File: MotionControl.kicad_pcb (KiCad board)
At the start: 2 copper layers, 180 x 80 mm, 180 parts, among them J1 Screw_Terminal_01x02, J10 Screw_Terminal_01x02, J11 Screw_Terminal_01x02, J12 Conn_01x07_MountingPin, J13 Conn_01x07_MountingPin, J14 Conn_01x07_MountingPin, J2 Conn_ARM_JTAG_SWD_10, J3 Screw_Terminal_01x04, J4 Conn_01x07_MountingPin, J5 Screw_Terminal_01x04, J6 Screw_Terminal_01x04, J7 Screw_Terminal_01x04, J8 Screw_Terminal_01x02, J9 Screw_Terminal_01x02, P1 USB_C_Plug_USB2.0, Q1 2N7002, Q10 Q_NMOS_DGS, Q11 Q_NMOS_DGS, Q12 Q_NMOS_DGS, Q13 Q_NMOS_DGS, Q14 Q_NMOS_DGS, Q15 Q_NMOS_DGS, Q16 Q_NMOS_DGS, Q17 Q_NMOS_DGS, Q18 Q_NMOS_DGS, Q19 Q_NMOS_DGS, Q2 Q_NMOS_DGS, Q20 Q_NMOS_DGS, Q21 Q_NMOS_DGS, Q22 Q_NMOS_DGS, Q23 Q_NMOS_DGS, Q24 Q_NMOS_DGS, Q25 Q_NMOS_DGS, Q26 Q_NMOS_DGS, Q27 Q_NMOS_DGS, Q28 Q_NMOS_DGS, Q29 Q_NMOS_DGS, Q3 Q_NMOS_DGS, Q30 Q_NMOS_DGS, Q31 Q_NMOS_DGS, Q32 Q_NMOS_DGS, Q33 Q_NMOS_DGS, Q4 Q_NMOS_DGS, Q5 Q_NMOS_DGS, Q6 Q_NMOS_DGS, Q7 Q_NMOS_DGS, Q8 Q_NMOS_DGS, Q9 Q_NMOS_DGS, SW1 SW_Push, U1 ATSAMD21J18A-A, U2 AP2112K-3.3, U3 TMC5160A-TA, U4 TMC5160A-TA, U5 TMC5160A-TA, U6 TMC5160A-TA, U7 TC4427, Y1 32.768kHz

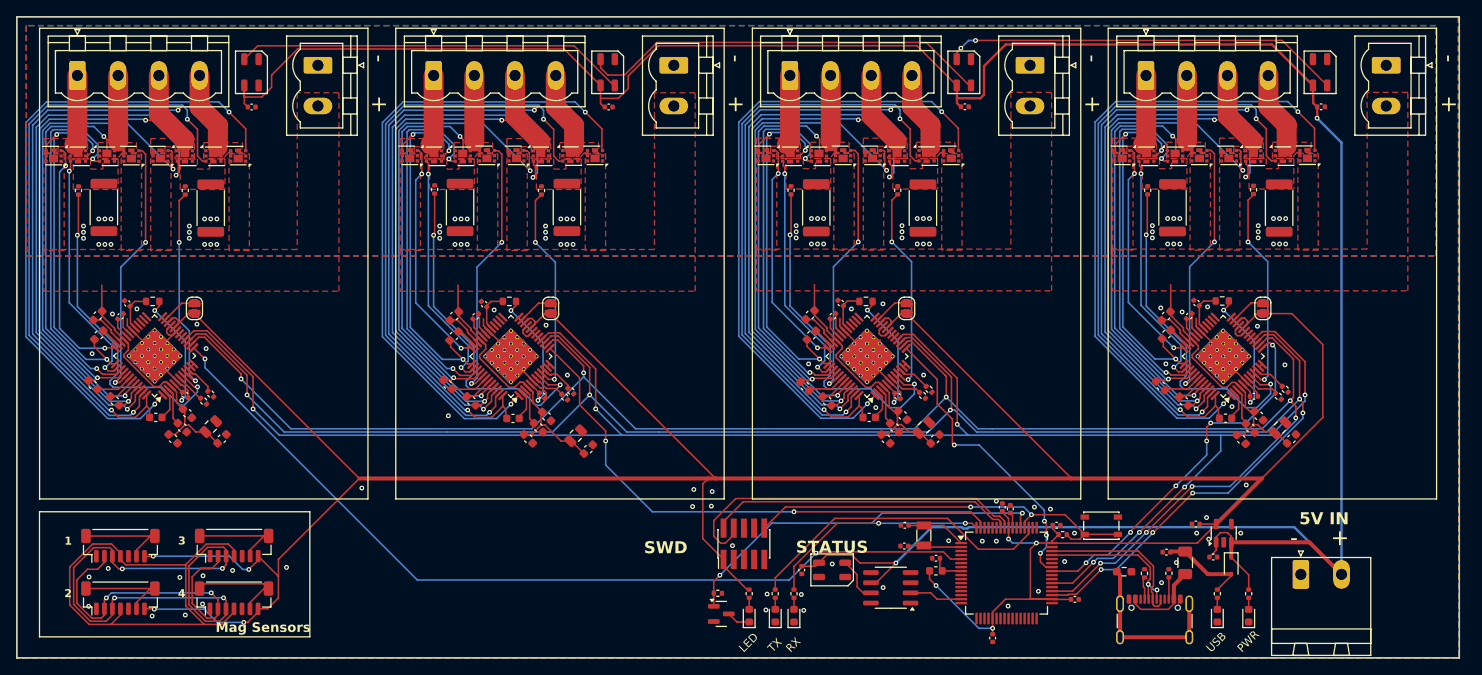
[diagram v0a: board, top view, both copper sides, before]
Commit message: begin work on optical inputs, finish mag sensors
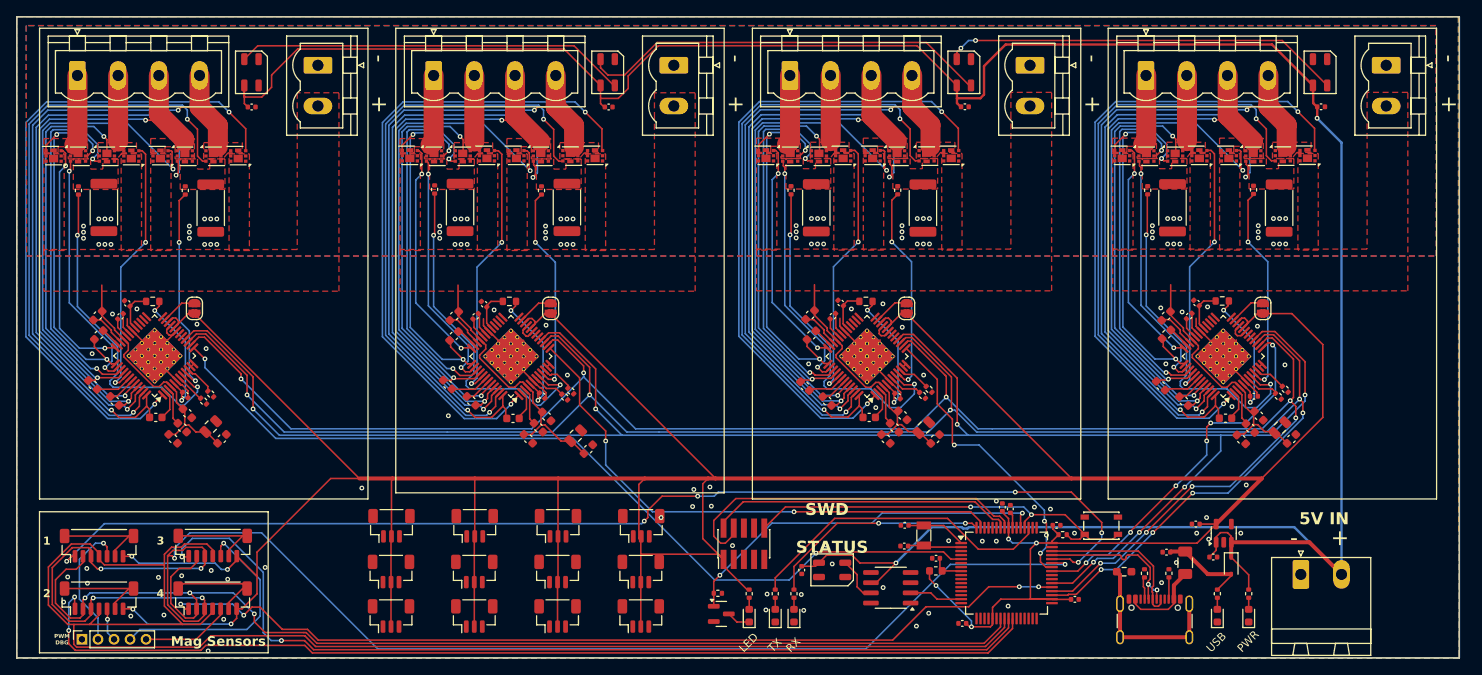
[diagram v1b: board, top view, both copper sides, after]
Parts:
- added J15: Conn_01x05_Pin, Connector_PinSocket_2.00mm:PinSocket_1x05_P2.00mm_Vertical, F.Cu at (41.1, 98.0)
- added J16: Conn_01x03_MountingPin, Connector_JST:JST_SH_BM03B-SRSS-TB_1x03-1MP_P1.00mm_Vertical, F.Cu at (79.8, 83.8)
- added J17: Conn_01x03_MountingPin, Connector_JST:JST_SH_BM03B-SRSS-TB_1x03-1MP_P1.00mm_Vertical, F.Cu at (79.7, 89.5)
- added J18: Conn_01x03_MountingPin, Connector_JST:JST_SH_BM03B-SRSS-TB_1x03-1MP_P1.00mm_Vertical, F.Cu at (79.7, 95.1)
- added J19: Conn_01x03_MountingPin, Connector_JST:JST_SH_BM03B-SRSS-TB_1x03-1MP_P1.00mm_Vertical, F.Cu at (90.2, 83.8)
- added J20: Conn_01x03_MountingPin, Connector_JST:JST_SH_BM03B-SRSS-TB_1x03-1MP_P1.00mm_Vertical, F.Cu at (90.1, 89.5)
- added J21: Conn_01x03_MountingPin, Connector_JST:JST_SH_BM03B-SRSS-TB_1x03-1MP_P1.00mm_Vertical, F.Cu at (90.1, 95.1)
- added J22: Conn_01x03_MountingPin, Connector_JST:JST_SH_BM03B-SRSS-TB_1x03-1MP_P1.00mm_Vertical, F.Cu at (100.6, 83.8)
- added J23: Conn_01x03_MountingPin, Connector_JST:JST_SH_BM03B-SRSS-TB_1x03-1MP_P1.00mm_Vertical, F.Cu at (100.5, 89.5)
- added J24: Conn_01x03_MountingPin, Connector_JST:JST_SH_BM03B-SRSS-TB_1x03-1MP_P1.00mm_Vertical, F.Cu at (100.5, 95.1)
- added J25: Conn_01x03_MountingPin, Connector_JST:JST_SH_BM03B-SRSS-TB_1x03-1MP_P1.00mm_Vertical, F.Cu at (110.9, 83.8)
- added J26: Conn_01x03_MountingPin, Connector_JST:JST_SH_BM03B-SRSS-TB_1x03-1MP_P1.00mm_Vertical, F.Cu at (110.9, 89.5)
- added J27: Conn_01x03_MountingPin, Connector_JST:JST_SH_BM03B-SRSS-TB_1x03-1MP_P1.00mm_Vertical, F.Cu at (110.9, 95.1)
- R8, R9: value 130R -> 165R
- moved C10 4.20 mm to (151.0, 96.0), turned to 180 degrees
- moved J12 2.67 mm to (57.5, 92.9)
- moved J13 2.67 mm to (43.3, 86.3)
- moved J14 2.67 mm to (43.3, 92.9)
- moved J4 2.67 mm to (57.5, 86.3)
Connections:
- J12 pad 1: /Mag Sensors/CSn4 -> PA18_MAG_CSn4
- J12 pad 2: /Mag Sensors/MOSI -> PB10_MAG_MOSI
- J12 pad 3: /Mag Sensors/MISO -> PA22_MAG_MISO
- J12 pad 4: /Mag Sensors/CLK -> PB11_MAG_SCK
- J13 pad 1: /Mag Sensors/CSn1 -> PA23_MAG_CSn1
- J13 pad 2: /Mag Sensors/MOSI -> PB10_MAG_MOSI
- J13 pad 3: /Mag Sensors/MISO -> PA22_MAG_MISO
- J13 pad 4: /Mag Sensors/CLK -> PB11_MAG_SCK
- J14 pad 1: /Mag Sensors/CSn2 -> PB13_MAG_CSn2
- J14 pad 2: /Mag Sensors/MOSI -> PB10_MAG_MOSI
- J14 pad 3: /Mag Sensors/MISO -> PA22_MAG_MISO
- J14 pad 4: /Mag Sensors/CLK -> PB11_MAG_SCK
- J4 pad 1: /Mag Sensors/CSn3 -> PB12_MAG_CSn3
- J4 pad 2: /Mag Sensors/MOSI -> PB10_MAG_MOSI
- J4 pad 3: /Mag Sensors/MISO -> PA22_MAG_MISO
- J4 pad 4: /Mag Sensors/CLK -> PB11_MAG_SCK
- U1 pad 23: unconnected-(U1-PB10-Pad23) -> PB10_MAG_MOSI
- U1 pad 24: unconnected-(U1-PB11-Pad24) -> PB11_MAG_SCK
- U1 pad 25: unconnected-(U1-PB12-Pad25) -> PB12_MAG_CSn3
- U1 pad 26: unconnected-(U1-PB13-Pad26) -> PB13_MAG_CSn2
- U1 pad 37: unconnected-(U1-PA18-Pad37) -> PA18_MAG_CSn4
- U1 pad 43: unconnected-(U1-PA22-Pad43) -> PA22_MAG_MISO
- U1 pad 44: unconnected-(U1-PA23-Pad44) -> PA23_MAG_CSn1
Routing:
- net PA22_MAG_MISO: track 0.00 -> 196.2 mm, vias 0 -> 6
- net PB11_MAG_SCK: track 0.00 -> 186.3 mm
- net PB10_MAG_MOSI: track 0.00 -> 149.5 mm, vias 0 -> 3
- net PA23_MAG_CSn1: track 0.00 -> 145.8 mm, vias 0 -> 6
- net PB13_MAG_CSn2: track 0.00 -> 128.9 mm, vias 0 -> 2
- net PB12_MAG_CSn3: track 0.00 -> 118.1 mm, vias 0 -> 2
- net PA18_MAG_CSn4: track 0.00 -> 115.4 mm, vias 0 -> 4
- net +3V3: track 405.9 -> 497.2 mm
- net /Mag Sensors/MISO: track 69.2 -> 0.00 mm, vias 4 -> 0
- net /Mag Sensors/CLK: track 63.6 -> 0.00 mm
- net /Mag Sensors/MOSI: track 43.3 -> 0.00 mm, vias 2 -> 0
- net /Mag Sensors/PWM3: track 0.00 -> 30.2 mm, vias 0 -> 1
- net /Mag Sensors/PWM1: track 0.00 -> 16.6 mm, vias 0 -> 1
- net /Mag Sensors/PWM4: track 0.00 -> 11.3 mm
- net /Mag Sensors/PWM2: track 0.00 -> 4.17 mm, vias 0 -> 1
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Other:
- board text added: "PWM DBG"

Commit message: cs routing changes, endstop stuff
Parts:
- moved J16 10.4 mm to (69.4, 83.8)
- moved J19 10.4 mm to (79.7, 83.8)
- moved J22 10.4 mm to (90.1, 83.8)
- moved J17 10.4 mm to (69.3, 89.5)
- moved J18 10.4 mm to (69.3, 95.1)
- moved J20 10.4 mm to (79.7, 89.5)
- moved J21 10.4 mm to (79.7, 95.1)
- moved J23 10.4 mm to (90.1, 89.5)
- moved J24 10.4 mm to (90.1, 95.1)
- moved J25 10.4 mm to (100.5, 83.8)
- moved J26 10.4 mm to (100.5, 89.5)
- moved J27 10.4 mm to (100.5, 95.1)
- moved C7 0.47 mm to (156.0, 81.1)
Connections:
- J13 pad 1: PA23_MAG_CSn1 -> PB30_MAG_CSn1
- J16 pad 3: /Optical Sensors/OUT1 -> PB00_ES1
- J17 pad 3: /Optical Sensors/OUT2 -> PB01_ES2
- J18 pad 3: /Optical Sensors/OUT3 -> PB05_ES3
- J19 pad 3: /Optical Sensors/OUT4 -> PB06_ES4
- J20 pad 3: /Optical Sensors/OUT5 -> PB07_ES5
- J21 pad 3: /Optical Sensors/OUT6 -> PB08_ES6
- J22 pad 3: /Optical Sensors/OUT7 -> PB06_ES7
- J23 pad 3: /Optical Sensors/OUT8 -> PB15_ES8
- J24 pad 3: /Optical Sensors/OUT9 -> PB16_ES9
- J25 pad 3: /Optical Sensors/OUT10 -> PB17_ES10
- J26 pad 3: /Optical Sensors/OUT11 -> PB22_ES11
- J27 pad 3: /Optical Sensors/OUT12 -> PB23_ES12
- U1 pad 10: unconnected-(U1-PB07-Pad10) -> PB07_ES5
- U1 pad 11: unconnected-(U1-PB08-Pad11) -> PB08_ES6
- U1 pad 12: unconnected-(U1-PB09-Pad12) -> PB06_ES7
- U1 pad 27: unconnected-(U1-PB14-Pad27) -> PA18_MAG_CSn4
- U1 pad 28: unconnected-(U1-PB15-Pad28) -> PB15_ES8
- U1 pad 37: PA18_MAG_CSn4 -> unconnected-(U1-PA18-Pad37)
- U1 pad 39: unconnected-(U1-PB16-Pad39) -> PB16_ES9
- U1 pad 40: unconnected-(U1-PB17-Pad40) -> PB17_ES10
- U1 pad 44: PA23_MAG_CSn1 -> unconnected-(U1-PA23-Pad44)
- U1 pad 49: unconnected-(U1-PB22-Pad49) -> PB22_ES11
- U1 pad 50: unconnected-(U1-PB23-Pad50) -> PB23_ES12
- U1 pad 59: unconnected-(U1-PB30-Pad59) -> PB30_MAG_CSn1
- U1 pad 6: unconnected-(U1-PB05-Pad6) -> PB05_ES3
- U1 pad 61: unconnected-(U1-PB00-Pad61) -> PB00_ES1
- U1 pad 62: unconnected-(U1-PB01-Pad62) -> PB01_ES2
- U1 pad 9: unconnected-(U1-PB06-Pad9) -> PB06_ES4
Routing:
- net PA23_MAG_CSn1: track 145.8 -> 0.00 mm, vias 6 -> 0
- net PB30_MAG_CSn1: track 0.00 -> 124.6 mm, vias 0 -> 6
- net +3V3: track 497.2 -> 487.1 mm
- net PA18_MAG_CSn4: track 115.4 -> 111.9 mm
- net PA28_LED: track 47.1 -> 50.1 mm
- net /RESETn: track 51.8 -> 53.4 mm
- net PB10_MAG_MOSI: track 149.5 -> 148.9 mm
- net PB13_MAG_CSn2: track 128.9 -> 129.5 mm
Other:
- board text added: "Endstops"
- board text added: "Mag Encoders"
- board text removed: "Mag Sensors"

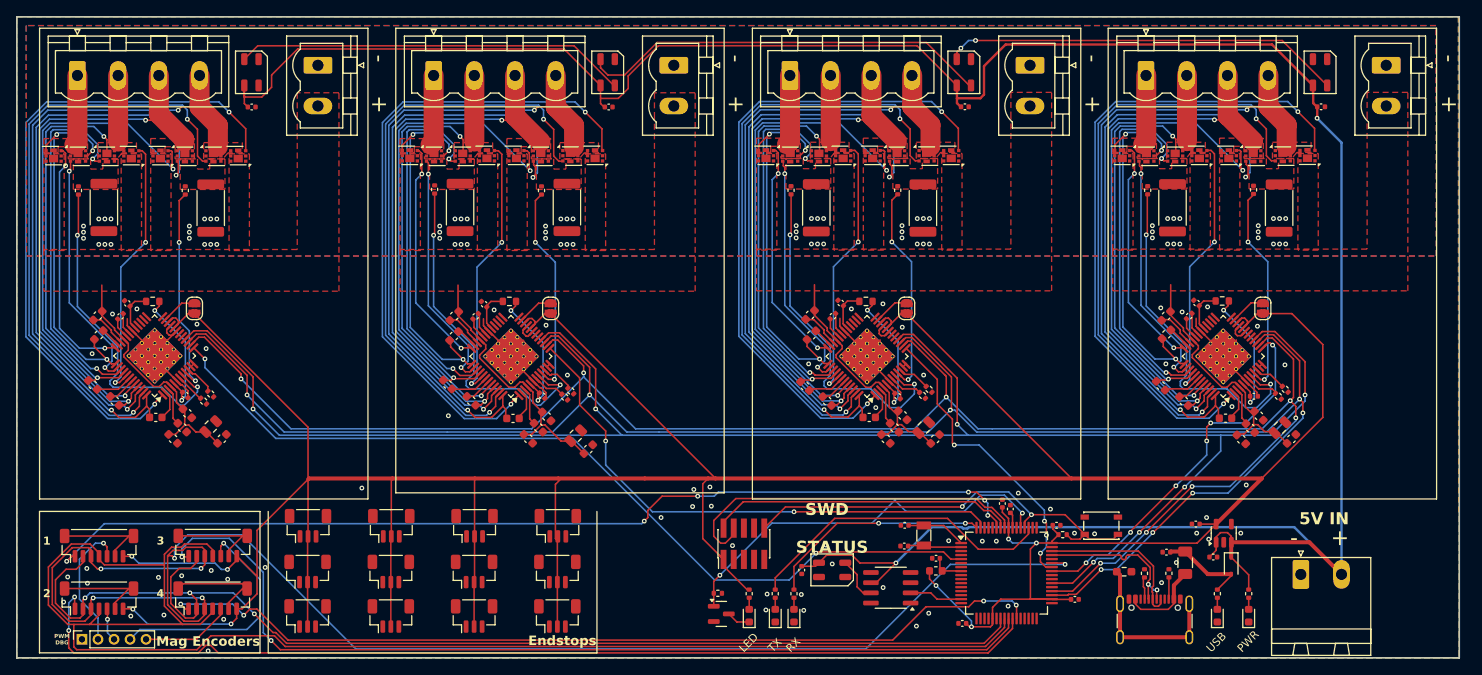
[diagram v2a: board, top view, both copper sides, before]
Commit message: route all endstops
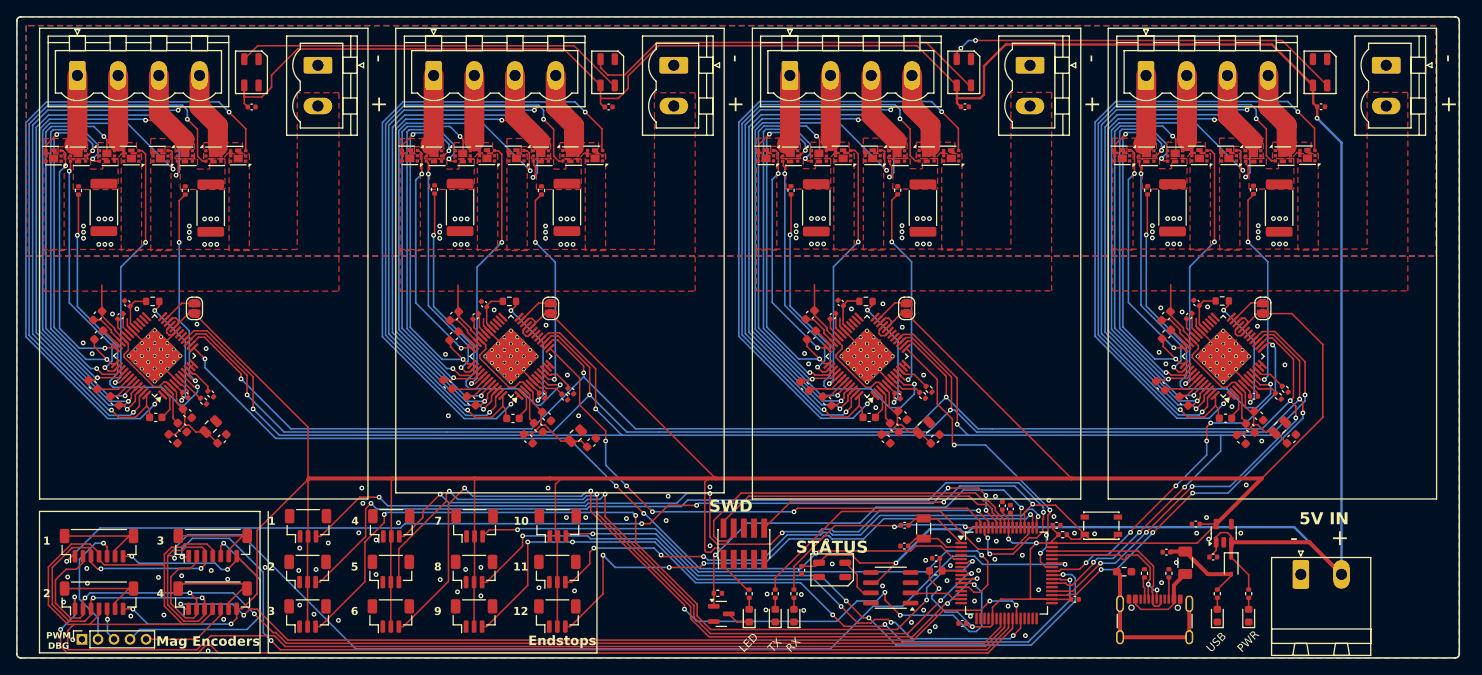
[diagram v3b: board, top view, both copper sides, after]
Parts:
- moved C48 0.92 mm to (104.7, 73.4)
- moved Y1 0.86 mm to (146.2, 84.2)
- moved C7 0.28 mm to (156.0, 81.3)
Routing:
- net PB01_ES2: track 0.00 -> 114.2 mm, vias 0 -> 4
- net PB08_ES6: track 0.00 -> 106.4 mm, vias 0 -> 6
- net PB05_ES3: track 0.00 -> 106.2 mm, vias 0 -> 4
- net PB00_ES1: track 0.00 -> 96.2 mm, vias 0 -> 4
- net PB07_ES5: track 0.00 -> 95.2 mm, vias 0 -> 4
- net PB16_ES9: track 0.00 -> 93.2 mm, vias 0 -> 5
- net PB06_ES4: track 0.00 -> 89.1 mm, vias 0 -> 4
- net PB15_ES8: track 0.00 -> 77.8 mm, vias 0 -> 4
- net PB17_ES10: track 0.00 -> 77.7 mm, vias 0 -> 4
- net PB06_ES7: track 0.00 -> 74.2 mm, vias 0 -> 2
- net PB23_ES12: track 0.00 -> 70.1 mm, vias 0 -> 4
- net PB22_ES11: track 0.00 -> 67.3 mm, vias 0 -> 4
- net /RESETn: track 53.4 -> 55.4 mm
- net +3V3: track 487.1 -> 489.0 mm
- net PA28_LED: track 50.1 -> 51.5 mm
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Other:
- outline, holes or cut-outs redrawn
- board text added: "10"
- board text added: "11"
- board text added: "12"
- board text added: "5"
- board text added: "6"
- board text added: "7"
- board text added: "8"
- board text added: "9"

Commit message: add spi master connector
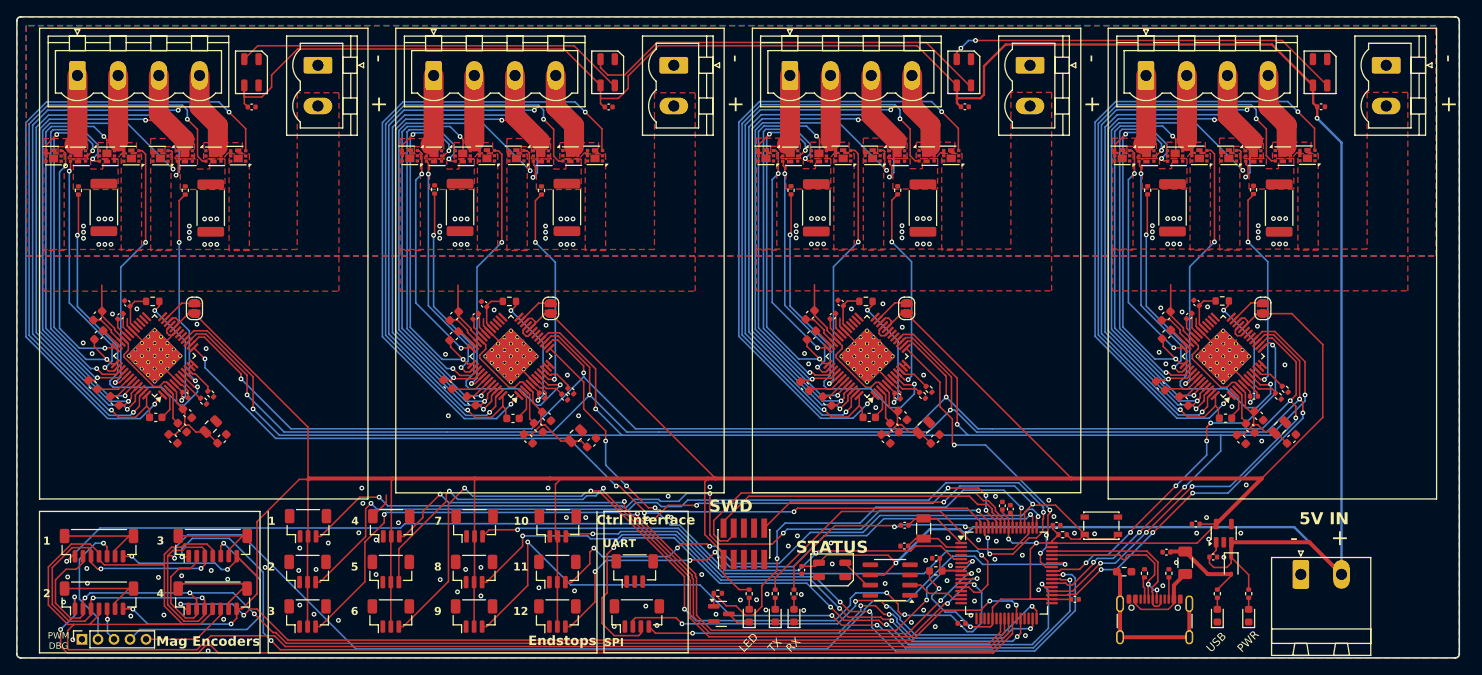
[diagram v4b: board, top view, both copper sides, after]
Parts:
- added J28: Conn_01x04_MountingPin, Connector_JST:JST_SH_BM04B-SRSS-TB_1x04-1MP_P1.00mm_Vertical, F.Cu at (110.4, 95.1)
- added J29: Conn_01x03_MountingPin, Connector_JST:JST_SH_BM03B-SRSS-TB_1x03-1MP_P1.00mm_Vertical, F.Cu at (110.1, 89.5)
- moved U7 0.97 mm to (142.0, 90.6)
- moved C10 0.10 mm to (150.9, 96.0)
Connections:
- U1 pad 31: unconnected-(U1-PA14-Pad31) -> PA14_MASTER_SCK
- U1 pad 32: unconnected-(U1-PA15-Pad32) -> PA15_MASTER_MOSI
- U1 pad 37: unconnected-(U1-PA18-Pad37) -> PA18_MASTER_MISO
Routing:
- net PA18_MASTER_MISO: track 0.00 -> 84.9 mm, vias 0 -> 4
- net PA15_MASTER_MOSI: track 0.00 -> 57.8 mm, vias 0 -> 4
- net PA14_MASTER_SCK: track 0.00 -> 53.5 mm, vias 0 -> 4
- net PA28_LED: track 51.5 -> 55.5 mm
- net GND: track 100.8 -> 104.1 mm, vias 179 -> 186
- net PB17_ES10: track 77.7 -> 80.3 mm
- net PB07_ES5: track 95.2 -> 96.7 mm
- net Net-(D11-DIN): track 5.66 -> 4.34 mm
- net PB16_ES9: track 93.2 -> 94.4 mm, vias 5 -> 4
- net PB22_ES11: track 67.3 -> 68.5 mm
- net /D-: track 20.2 -> 21.3 mm
- net /D+: track 20.1 -> 21.2 mm
- net PB23_ES12: track 70.1 -> 69.3 mm
- net PB15_ES8: track 77.8 -> 78.5 mm
- net PB08_ES6: track 106.4 -> 107.0 mm
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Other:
- board text added: "Ctrl Interface"
- board text added: "SPI"
- board text added: "UART"
